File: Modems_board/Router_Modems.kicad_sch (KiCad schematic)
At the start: 34 parts

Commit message: routing procs
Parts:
- removed X?: Bus_M.2_Socket_B, symbol Connector:Bus_M.2_Socket_B
- added C18, C19: 4.7u, Capacitor_SMD:C_1206_3216Metric, symbol Device:C
- added C20: 910p, Capacitor_SMD:C_0603_1608Metric, symbol Device:C
- added C21: 6.8p, Capacitor_SMD:C_0603_1608Metric, symbol Device:C
- added C22, C27, C28, C32, C33: 0.1u, Capacitor_SMD:C_0603_1608Metric, symbol Device:C
- added C23, C30: 1u, Capacitor_SMD:C_0603_1608Metric, symbol Device:C
- added C24, C26: 100u, Capacitor_Tantalum_SMD:CP_EIA-3528-15_AVX-H, symbol Device:C_Polarized
- added C25, C29, C31, C34: 47u, Capacitor_SMD:C_1206_3216Metric, symbol Device:C
- added D1, D3, D5, D6: LED, LED_THT:LED_D3.0mm, symbol Device:LED
- added D4: SS510, Diode_SMD:D_SMA, symbol Device:D_Schottky
- added H1, H2, H3, H4, H5, H6: M3, MountingHole:MountingHole_3.5mm_Pad, symbol Mechanical:MountingHole_Pad
- added L2: 15uH, Inductor_SMD:L_Sunlord_MWSA1004S, symbol Device:L
- added N1, N2, N3, N4: SMTSO2515CTJ, MountingHole:MountingHole_3.2mm_M3_Pad, symbol Mechanical:MountingHole_Pad
- added R10, R12: 47k, Resistor_SMD:R_0603_1608Metric, symbol Device:R
- added R11, R15: 2k, Resistor_SMD:R_0603_1608Metric, symbol Device:R
- added R13: 15k, Resistor_SMD:R_0603_1608Metric, symbol Device:R
- added R14, R16, R3, R8: 470, Resistor_SMD:R_0603_1608Metric, symbol Device:R
- added R9: 200k, Resistor_SMD:R_0603_1608Metric, symbol Device:R
- added U4: TPS54540, Package_SO:TI_SO-PowerPAD-8_ThermalVias, symbol Regulator_Switching:TPS54360DDA
- added U5, U6: SRV05-4, Package_TO_SOT_SMD:SOT-23-6, symbol Power_Protection:SRV05-4
- added X10, X6: SIM_Card, proj:FCI_7111S2015X02LF, symbol Connector:SIM_Card
- added X11, X5, X7: Bus_M.2_Socket_B, proj:AMPHENOL_MDT420B03001, symbol Connector:Bus_M.2_Socket_B
- added X12, X13: S4B-XH, Connector_JST:JST_XH_S4B-XH-A_1x04_P2.50mm_Horizontal, symbol Connector_Generic:Conn_01x04
- added X2: B2B-XH, Connector_JST:JST_XH_B2B-XH-A_1x02_P2.50mm_Vertical, symbol Connector_Generic:Conn_01x02
- C1, C11, C15, C16, C3, C5: renamed from C?; footprint (none) -> Capacitor_SMD:C_0603_1608Metric
- C12, C14: renamed from C?; footprint (none) -> Capacitor_Tantalum_SMD:CP_EIA-3528-15_AVX-H
- C13, C17, C2, C4, C6, C7: renamed from C?; footprint (none) -> Capacitor_SMD:C_1206_3216Metric
- C8: renamed from C?; value 820p -> 910p
- L1: renamed from L?; footprint Inductor_SMD:L_Abracon_ASPI-0630LR -> Inductor_SMD:L_Sunlord_MWSA1004S
- R1, R5: renamed from R?; value 4.7k -> 2k; footprint (none) -> Resistor_SMD:R_0603_1608Metric
- R4: renamed from R?; value 56k -> 47k
- X1, X4: renamed from X?; footprint (none) -> proj:FCI_7111S2015X02LF
- X3: renamed from X?; footprint (none) -> proj:AMPHENOL_MDT420B03001
- X8, X9: renamed from X?; value B4B-XH -> S4B-XH; footprint (none) -> Connector_JST:JST_XH_S4B-XH-A_1x04_P2.50mm_Horizontal
- gave numbers to parts that had none: 9
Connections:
- net GND: now also X3.P1 (MP), X3.P2 (MP), X8.1 (Pin_1), X9.1 (Pin_1), C18.2, C19.2, C20.2, C21.1, C23.2, C24.2, C25.2, C26.2, C27.2, C28.2, C29.2, C30.2, C31.2, C32.2, C33.2, C34.2, D4.2 (A), H1.1, H2.1, H3.1, H4.1, H5.1, H6.1, N1.1, N2.1, N3.1, N4.1, R13.2, R9.2, U4.7 (GND), U4.9 (GNDPAD), U5.2 (VN), U6.2 (VN), X10.5 (GND), X11.11 (GND), X11.27 (GND), X11.3 (GND), X11.33 (GND), X11.39 (GND), X11.45 (GND), X11.5 (GND), X11.51 (GND), X11.57 (GND), X11.71 (GND), X11.73 (GND), X11.P1 (MP), X11.P2 (MP), X12.1 (Pin_1), X13.1 (Pin_1), X2.1 (Pin_1), X5.11 (GND), X5.27 (GND), X5.3 (GND), X5.33 (GND), X5.39 (GND), X5.45 (GND), X5.5 (GND), X5.51 (GND), X5.57 (GND), X5.71 (GND), X5.73 (GND), X5.P1 (MP), X5.P2 (MP), X6.5 (GND), X7.11 (GND), X7.27 (GND), X7.3 (GND), X7.33 (GND), X7.39 (GND), X7.45 (GND), X7.5 (GND), X7.51 (GND), X7.57 (GND), X7.71 (GND), X7.73 (GND), X7.P1 (MP), X7.P2 (MP); no longer X8.4 (Pin_4), X9.4 (Pin_4)
- net SIM2_CLK: now also X5.32 (UIM-CLK)
- net SIM2_DAT: now also X5.34 (UIM-DATA)
- net SIM2_PWR: now also X5.36 (UIM-PWR)
- net SIM2_RST: now also X5.30 (UIM-RESET)
- net USB1_N: now also X8.3 (Pin_3); no longer X8.2 (Pin_2)
- net USB1_P: now also X8.2 (Pin_2); no longer X8.3 (Pin_3)
- net USB2_N: now also X9.3 (Pin_3), X5.9 (USB_D-); no longer X9.2 (Pin_2)
- net USB2_P: now also X9.2 (Pin_2), X5.7 (USB_D+); no longer X9.3 (Pin_3)
- net VCC: now also C18.1, C19.1, U4.2 (VIN), X2.2 (Pin_2); no longer X8.1 (Pin_1), X9.1 (Pin_1)
- net M1_ONOFF: now reaches R1.2, X3.6 (~{FULL_CARD_POWER_OFF})
- net M1_ONOFF: now also X8.4 (Pin_4)
- net at X3.10 (GPIO_9/DAS/~{DSS}/~{LED1}): now also R3.1
- net M2_ONOFF: now reaches R5.2
- net M2_ONOFF: now also X9.4 (Pin_4), X5.6 (~{FULL_CARD_POWER_OFF})
- net +3V3 renamed +3V3A
- net +3V3A: now also C24.1, C26.1, D1.2 (A), D3.2 (A), L2.2, R12.1, X5.2 (3.3V), X5.4 (3.3V), X5.70 (3.3V), X5.72 (3.3V), X5.74 (3.3V)
- new net: D5.1 (K), R14.2
- new net: C21.2, R10.1, U4.6 (COMP)
- new net: C20.1, R10.2
- new net: R9.1, U4.4 (RT/CLK)
- new net: R16.1, X11.10 (GPIO_9/DAS/~{DSS}/~{LED1})
- new net: R8.1, X5.10 (GPIO_9/DAS/~{DSS}/~{LED1})
- new net: D3.1 (K), R8.2
- new net: C22.2, D4.1 (K), L2.1, U4.8 (SW)
- new net: C22.1, U4.1 (BOOT)
- new net: R12.2, R13.1, U4.5 (FB)
- new net: D6.1 (K), R16.2
- new net: R14.1, X7.10 (GPIO_9/DAS/~{DSS}/~{LED1})
- new net: D1.1 (K), R3.2
- new net +3V3B: C25.1, C27.1, C28.1, C29.1, C31.1, C32.1, C33.1, C34.1, D5.2 (A), D6.2 (A), R11.1, R15.1, X11.2 (3.3V), X11.4 (3.3V), X11.70 (3.3V), X11.72 (3.3V), X11.74 (3.3V), X7.2 (3.3V), X7.4 (3.3V), X7.70 (3.3V), X7.72 (3.3V), X7.74 (3.3V)
- new net M3_ONOFF: R11.2, X12.4 (Pin_4), X7.6 (~{FULL_CARD_POWER_OFF})
- new net M4_ONOFF: R15.2, X11.6 (~{FULL_CARD_POWER_OFF}), X13.4 (Pin_4)
- new net SIM3_CLK: U5.3 (IO2), X6.3 (CLK), X7.32 (UIM-CLK)
- new net SIM3_DAT: U5.1 (IO1), X6.7 (I/O), X7.34 (UIM-DATA)
- new net SIM3_PWR: C23.1, U5.5 (VP), X6.1 (VCC), X7.36 (UIM-PWR)
- new net SIM3_RST: U5.4 (IO3), X6.2 (RST), X7.30 (UIM-RESET)
- new net SIM4_CLK: U6.3 (IO2), X10.3 (CLK), X11.32 (UIM-CLK)
- new net SIM4_DAT: U6.1 (IO1), X10.7 (I/O), X11.34 (UIM-DATA)
- new net SIM4_PWR: C30.1, U6.5 (VP), X10.1 (VCC), X11.36 (UIM-PWR)
- new net SIM4_RST: U6.4 (IO3), X10.2 (RST), X11.30 (UIM-RESET)
- new net USB3_N: X12.3 (Pin_3), X7.9 (USB_D-)
- new net USB3_P: X12.2 (Pin_2), X7.7 (USB_D+)
- new net USB4_N: X11.9 (USB_D-), X13.3 (Pin_3)
- new net USB4_P: X11.7 (USB_D+), X13.2 (Pin_2)
- no-connect marks 87 -> 174
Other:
- moved on the sheet: C1, C10, C11, C12, C13, C14, C15, C16, C17, C2, C3, C4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

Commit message: routing procs
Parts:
- removed H6: M3, MountingHole:MountingHole_3.5mm_Pad, symbol Mechanical:MountingHole_Pad
- X12, X13, X8, X9: value S4B-XH -> B4B-XH; footprint Connector_JST:JST_XH_S4B-XH-A_1x04_P2.50mm_Horizontal -> Connector_JST:JST_XH_B4B-XH-A_1x04_P2.50mm_Vertical
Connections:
- net SIM1_CLK: now also U1.1 (IO1); no longer U1.3 (IO2)
- net SIM1_DAT: now also U1.4 (IO3); no longer U1.1 (IO1)
- net SIM1_RST: now also U1.6 (IO4); no longer U1.4 (IO3)
- net SIM2_CLK: now also U3.1 (IO1); no longer U3.3 (IO2)
- net SIM2_DAT: now also U3.4 (IO3); no longer U3.1 (IO1)
- net SIM2_RST: now also U3.6 (IO4); no longer U3.4 (IO3)
- net SIM3_CLK: now also U5.1 (IO1); no longer U5.3 (IO2)
- net SIM3_DAT: now also U5.4 (IO3); no longer U5.1 (IO1)
- net SIM3_RST: now also U5.6 (IO4); no longer U5.4 (IO3)
- net SIM4_CLK: now also U6.1 (IO1); no longer U6.3 (IO2)
- net SIM4_DAT: now also U6.4 (IO3); no longer U6.1 (IO1)
- net SIM4_RST: now also U6.6 (IO4); no longer U6.4 (IO3)

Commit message: Modems board ready
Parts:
- added C35, C36: 100u, Capacitor_Tantalum_SMD:CP_EIA-3528-15_AVX-H, symbol Device:C_Polarized
- added C37: 100u 50V, Capacitor_SMD:CP_Elec_10x10.5, symbol Device:C_Polarized
- R10, R4: value 47k -> 43k
- R14, R16, R3, R8: value 470 -> 470R
- X11, X3, X5, X7: value Bus_M.2_Socket_B -> AS0BC21-S30BB-7H
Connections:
- net +3V3A: now also C36.1; no longer C12.1, C14.1, L1.2, R6.1
- net +3V3B: now also C12.1, C14.1, L1.2, R6.1, C35.1
- net GND: now also C35.2, C36.2, C37.2
- net VCC: now also C37.1
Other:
- moved on the sheet: X2

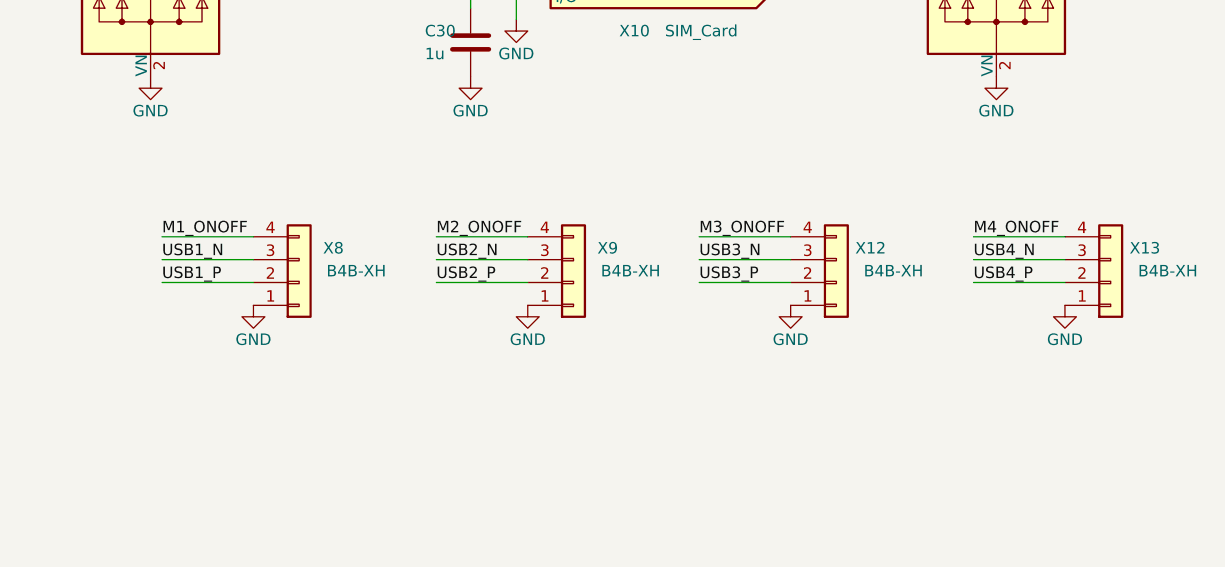
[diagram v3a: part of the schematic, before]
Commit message: remove modems gpio ctrls
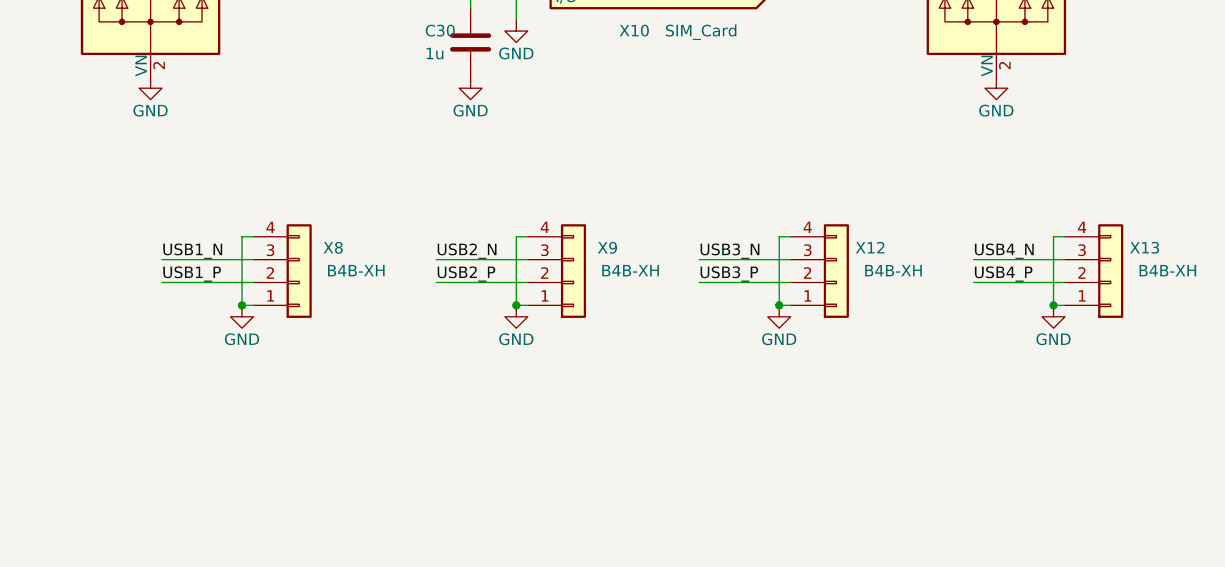
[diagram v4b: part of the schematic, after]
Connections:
- net GND: now also X12.4 (Pin_4), X13.4 (Pin_4), X8.4 (Pin_4), X9.4 (Pin_4)
- net M1_ONOFF: no longer X8.4 (Pin_4)
- net M2_ONOFF: no longer X9.4 (Pin_4)
- net M3_ONOFF: no longer X12.4 (Pin_4)
- net M4_ONOFF: no longer X13.4 (Pin_4)
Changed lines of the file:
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@@
   (junction (at 260.35 146.05) (diameter 0) (color 0 0 0 0)
   )
+  (junction (at 386.08 201.93) (diameter 0) (color 0 0 0 0)
+  )
   (junction (at 264.16 146.05) (diameter 0) (color 0 0 0 0)
   )
@@
   (junction (at 347.98 146.05) (diameter 0) (color 0 0 0 0)
   )
+  (junction (at 326.39 201.93) (diameter 0) (color 0 0 0 0)
+  )
   (junction (at 218.44 257.81) (diameter 0) (color 0 0 0 0)
   )
@@
   )
   (junction (at 67.31 226.06) (diameter 0) (color 0 0 0 0)
+  )
+  (junction (at 295.91 201.93) (diameter 0) (color 0 0 0 0)
+  )
+  (junction (at 355.6 201.93) (diameter 0) (color 0 0 0 0)
   )
   (junction (at 143.51 231.14) (diameter 0) (color 0 0 0 0)
@@
     (stroke (width 0) (type default) (color 0 0 0 0))
   )
+  (wire (pts (xy 327.66 194.31) (xy 326.39 194.31))
+    (stroke (width 0) (type default) (color 0 0 0 0))
+  )
   (wire (pts (xy 255.27 232.41) (xy 248.92 232.41))
     (stroke (width 0) (type default) (color 0 0 0 0))
@@
     (stroke (width 0) (type default) (color 0 0 0 0))
   )
+  (wire (pts (xy 387.35 194.31) (xy 386.08 194.31))
+    (stroke (width 0) (type default) (color 0 0 0 0))
+  )
   (wire (pts (xy 45.72 233.68) (xy 45.72 228.6))
     (stroke (width 0) (type default) (color 0 0 0 0))
@@
     (stroke (width 0) (type default) (color 0 0 0 0))
   )
-  (wire (pts (xy 346.71 194.31) (xy 356.87 194.31))
+  (wire (pts (xy 355.6 201.93) (xy 356.87 201.93))
     (stroke (width 0) (type default) (color 0 0 0 0))
   )
@@
     (stroke (width 0) (type default) (color 0 0 0 0))
   )
+  (wire (pts (xy 297.18 194.31) (xy 295.91 194.31))
+    (stroke (width 0) (type default) (color 0 0 0 0))
+  )
   (wire (pts (xy 317.5 196.85) (xy 327.66 196.85))
     (stroke (width 0) (type default) (color 0 0 0 0))
@@
     (stroke (width 0) (type default) (color 0 0 0 0))
   )
+  (wire (pts (xy 355.6 194.31) (xy 355.6 201.93))
+    (stroke (width 0) (type default) (color 0 0 0 0))
+  )
   (wire (pts (xy 233.68 163.83) (xy 232.41 163.83))
     (stroke (width 0) (type default) (color 0 0 0 0))
   )
+  (wire (pts (xy 326.39 194.31) (xy 326.39 201.93))
+    (stroke (width 0) (type default) (color 0 0 0 0))
+  )
   (wire (pts (xy 217.17 168.91) (xy 233.68 168.91))
     (stroke (width 0) (type default) (color 0 0 0 0))
@@
     (stroke (width 0) (type default) (color 0 0 0 0))
   )
+  (wire (pts (xy 295.91 201.93) (xy 297.18 201.93))
+    (stroke (width 0) (type default) (color 0 0 0 0))
+  )
   (wire (pts (xy 306.07 125.73) (xy 322.58 125.73))
     (stroke (width 0) (type default) (color 0 0 0 0))
@@
     (stroke (width 0) (type default) (color 0 0 0 0))
   )
-  (wire (pts (xy 287.02 194.31) (xy 297.18 194.31))
-    (stroke (width 0) (type default) (color 0 0 0 0))
-  )
   (wire (pts (xy 78.74 231.14) (xy 78.74 232.41))
     (stroke (width 0) (type default) (color 0 0 0 0))
@@
     (stroke (width 0) (type default) (color 0 0 0 0))
   )
-  (wire (pts (xy 377.19 194.31) (xy 387.35 194.31))
-    (stroke (width 0) (type default) (color 0 0 0 0))
-  )
   (wire (pts (xy 124.46 154.94) (xy 124.46 168.91))
     (stroke (width 0) (type default) (color 0 0 0 0))
@@
     (stroke (width 0) (type default) (color 0 0 0 0))
   )
+  (wire (pts (xy 386.08 201.93) (xy 387.35 201.93))
+    (stroke (width 0) (type default) (color 0 0 0 0))
+  )
   (wire (pts (xy 210.82 224.79) (xy 223.52 224.79))
     (stroke (width 0) (type default) (color 0 0 0 0))
   )
+  (wire (pts (xy 386.08 194.31) (xy 386.08 201.93))
+    (stroke (width 0) (type default) (color 0 0 0 0))
+  )
   (wire (pts (xy 217.17 156.21) (xy 227.33 156.21))
     (stroke (width 0) (type default) (color 0 0 0 0))
@@
     (stroke (width 0) (type default) (color 0 0 0 0))
   )
+  (wire (pts (xy 326.39 201.93) (xy 327.66 201.93))
+    (stroke (width 0) (type default) (color 0 0 0 0))
+  )
   (wire (pts (xy 218.44 257.81) (xy 223.52 257.81))
     (stroke (width 0) (type default) (color 0 0 0 0))
@@
     (stroke (width 0) (type default) (color 0 0 0 0))
   )
+  (wire (pts (xy 295.91 194.31) (xy 295.91 201.93))
+    (stroke (width 0) (type default) (color 0 0 0 0))
+  )
   (wire (pts (xy 248.92 38.1) (xy 255.27 38.1))
     (stroke (width 0) (type default) (color 0 0 0 0))
@@
     (stroke (width 0) (type default) (color 0 0 0 0))
   )
-  (wire (pts (xy 317.5 194.31) (xy 327.66 194.31))
-    (stroke (width 0) (type default) (color 0 0 0 0))
-  )
   (wire (pts (xy 20.32 158.75) (xy 36.83 158.75))
     (stroke (width 0) (type default) (color 0 0 0 0))
@@
     (stroke (width 0) (type default) (color 0 0 0 0))
   )
+  (wire (pts (xy 356.87 194.31) (xy 355.6 194.31))
+    (stroke (width 0) (type default) (color 0 0 0 0))
+  )
   (wire (pts (xy 353.06 38.1) (xy 359.41 38.1))
     (stroke (width 0) (type default) (color 0 0 0 0))
@@
     (effects (font (size 1.27 1.27)) (justify left bottom))
   )
-  (label "M3_ONOFF" (at 346.71 194.31 0)
-    (effects (font (size 1.27 1.27)) (justify left bottom))
-  )
   (label "SIM3_PWR" (at 275.59 151.13 0)
     (effects (font (size 1.27 1.27)) (justify left bottom))
@@
     (effects (font (size 1.27 1.27)) (justify left bottom))
   )
-  (label "M4_ONOFF" (at 377.19 194.31 0)
-    (effects (font (size 1.27 1.27)) (justify left bottom))
-  )
   (label "SIM1_PWR" (at 20.32 156.21 0)
     (effects (font (size 1.27 1.27)) (justify left bottom))
@@
   )
   (label "SIM1_DAT" (at 26.67 110.49 0)
-    (effects (font (size 1.27 1.27)) (justify left bottom))
-  )
-  (label "M1_ONOFF" (at 287.02 194.31 0)
     (effects (font (size 1.27 1.27)) (justify left bottom))
   )
@@
   )
   (label "USB3_P" (at 226.06 87.63 0)
-    (effects (font (size 1.27 1.27)) (justify left bottom))
-  )
-  (label "M2_ONOFF" (at 317.5 194.31 0)
     (effects (font (size 1.27 1.27)) (justify left bottom))
   )
@@
     (pin "2")
   )
-  (symbol (lib_id "power:GND") (at 297.18 201.93 0) (unit 1)
-    (in_bom yes) (on_board yes)
-    (property "Reference" "#PWR055" (id 0) (at 297.18 208.28 0)
-      (effects (font (size 1.27 1.27)) hide)
-    )
-    (property "Value" "GND" (id 1) (at 297.18 205.74 0))
-    (property "Footprint" "" (id 2) (at 297.18 201.93 0)
-      (effects (font (size 1.27 1.27)) hide)
-    )
-    (property "Datasheet" "" (id 3) (at 297.18 201.93 0)
+  (symbol (lib_id "power:GND") (at 295.91 201.93 0) (unit 1)
+    (in_bom yes) (on_board yes)
+    (property "Reference" "#PWR055" (id 0) (at 295.91 208.28 0)
+      (effects (font (size 1.27 1.27)) hide)
+    )
+    (property "Value" "GND" (id 1) (at 295.91 205.74 0))
+    (property "Footprint" "" (id 2) (at 295.91 201.93 0)
+      (effects (font (size 1.27 1.27)) hide)
+    )
+    (property "Datasheet" "" (id 3) (at 295.91 201.93 0)
       (effects (font (size 1.27 1.27)) hide)
     )
@@
     (pin "2")
   )
-  (symbol (lib_id "power:GND") (at 327.66 201.93 0) (unit 1)
-    (in_bom yes) (on_board yes)
-    (property "Reference" "#PWR059" (id 0) (at 327.66 208.28 0)
-      (effects (font (size 1.27 1.27)) hide)
-    )
-    (property "Value" "GND" (id 1) (at 327.66 205.74 0))
-    (property "Footprint" "" (id 2) (at 327.66 201.93 0)
-      (effects (font (size 1.27 1.27)) hide)
-    )
-    (property "Datasheet" "" (id 3) (at 327.66 201.93 0)
+  (symbol (lib_id "power:GND") (at 326.39 201.93 0) (unit 1)
+    (in_bom yes) (on_board yes)
+    (property "Reference" "#PWR059" (id 0) (at 326.39 208.28 0)
+      (effects (font (size 1.27 1.27)) hide)
+    )
+    (property "Value" "GND" (id 1) (at 326.39 205.74 0))
+    (property "Footprint" "" (id 2) (at 326.39 201.93 0)
+      (effects (font (size 1.27 1.27)) hide)
+    )
+    (property "Datasheet" "" (id 3) (at 326.39 201.93 0)
       (effects (font (size 1.27 1.27)) hide)
     )
@@
     (pin "2")
   )
-  (symbol (lib_id "power:GND") (at 387.35 201.93 0) (unit 1)
-    (in_bom yes) (on_board yes)
-    (property "Reference" "#PWR070" (id 0) (at 387.35 208.28 0)
-      (effects (font (size 1.27 1.27)) hide)
-    )
-    (property "Value" "GND" (id 1) (at 387.35 205.74 0))
-    (property "Footprint" "" (id 2) (at 387.35 201.93 0)
-      (effects (font (size 1.27 1.27)) hide)
-    )
-    (property "Datasheet" "" (id 3) (at 387.35 201.93 0)
+  (symbol (lib_id "power:GND") (at 386.08 201.93 0) (unit 1)
+    (in_bom yes) (on_board yes)
+    (property "Reference" "#PWR070" (id 0) (at 386.08 208.28 0)
+      (effects (font (size 1.27 1.27)) hide)
+    )
+    (property "Value" "GND" (id 1) (at 386.08 205.74 0))
+    (property "Footprint" "" (id 2) (at 386.08 201.93 0)
+      (effects (font (size 1.27 1.27)) hide)
+    )
+    (property "Datasheet" "" (id 3) (at 386.08 201.93 0)
       (effects (font (size 1.27 1.27)) hide)
     )
@@
     (pin "2")
   )
-  (symbol (lib_id "power:GND") (at 356.87 201.93 0) (unit 1)
-    (in_bom yes) (on_board yes)
-    (property "Reference" "#PWR066" (id 0) (at 356.87 208.28 0)
-      (effects (font (size 1.27 1.27)) hide)
-    )
-    (property "Value" "GND" (id 1) (at 356.87 205.74 0))
-    (property "Footprint" "" (id 2) (at 356.87 201.93 0)
-      (effects (font (size 1.27 1.27)) hide)
-    )
-    (property "Datasheet" "" (id 3) (at 356.87 201.93 0)
-      (effects (font (size 1.27 1.27)) hide)
-    )
+  (symbol (lib_id "power:GND") (at 355.6 201.93 0) (unit 1)
+    (in_bom yes) (on_board yes)
+    (property "Reference" "#PWR066" (id 0) (at 355.6 208.28 0)
+      (effects (font (size 1.27 1.27)) hide)
+    )
+    (property "Value" "GND" (id 1) (at 355.6 205.74 0))
+    (property "Footprint" "" (id 2) (at 355.6 201.93 0)
+      (effects (font (size 1.27 1.27)) hide)
+    )
+    (property "Datasheet" "" (id 3) (at 355.6 201.93 0)
+      (effects (font (size 1.27 1.27)) hide)
+    )
